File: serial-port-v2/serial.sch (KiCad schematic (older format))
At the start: 25 parts, among them J1 12V Pwr, J2 Serial, J3 XL-320, J4 AX-12A, J5 XL-320, J6 AX-12A, Q1 BSS138, U1 AP1117-50, U2 LM317, U4 74LVC1G126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

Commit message: board fixes
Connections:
- net +3V3: now also Q1.1 (G)
- net at Q1.2 (S), R5.2, U4.2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: no longer Q1.1 (G)
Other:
- moved on the sheet: R5
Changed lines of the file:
@@
 $EndComp
 Wire Wire Line
-	3350 5600 3350 5450
+	3350 5450 3350 5600
 Text GLabel 5350 1000 2    60   Output ~ 0
 RXI
@@
 L +3.3V #PWR027
 U 1 1 5A9E1497
-P 5300 4200
-F 0 "#PWR027" H 5300 4050 50  0001 C CNN
-F 1 "+3.3V" H 5300 4340 50  0000 C CNN
-F 2 "" H 5300 4200 50  0001 C CNN
-F 3 "" H 5300 4200 50  0001 C CNN
-	1    5300 4200
+P 5300 4400
+F 0 "#PWR027" H 5300 4250 50  0001 C CNN
+F 1 "+3.3V" H 5300 4540 50  0000 C CNN
+F 2 "" H 5300 4400 50  0001 C CNN
+F 3 "" H 5300 4400 50  0001 C CNN
+	1    5300 4400
 	-1   0    0    -1
 $EndComp
@@
 L R R5
 U 1 1 5A9E149D
-P 5300 4450
-F 0 "R5" V 5380 4450 50  0000 C CNN
-F 1 "10k" V 5300 4450 50  0000 C CNN
-F 2 "Resistors_SMD:R_1206_HandSoldering" V 5230 4450 50  0001 C CNN
-F 3 "" H 5300 4450 50  0001 C CNN
-	1    5300 4450
+P 5300 4750
+F 0 "R5" V 5380 4750 50  0000 C CNN
+F 1 "10k" V 5300 4750 50  0000 C CNN
+F 2 "Resistors_SMD:R_1206_HandSoldering" V 5230 4750 50  0001 C CNN
+F 3 "" H 5300 4750 50  0001 C CNN
+	1    5300 4750
 	-1   0    0    -1
 $EndComp
@@
 	5250 5000 5450 5000
 Wire Wire Line
-	5300 4200 5300 4300
-Wire Wire Line
-	5300 4600 5300 5000
+	5300 4400 5300 4600
+Wire Wire Line
+	5300 4900 5300 5000
 Connection ~ 5300 5000
 Wire Wire Line
-	5050 4700 5050 4650
-Wire Wire Line
-	5050 4650 5300 4650
-Connection ~ 5300 4650
+	5050 4500 5050 4700
 Wire Wire Line
 	4650 5000 4850 5000
@@
 	3600 5550 3350 5550
 Connection ~ 3350 5550
+Wire Wire Line
+	5050 4500 5300 4500
+Connection ~ 5300 4500
 $EndSCHEMATC

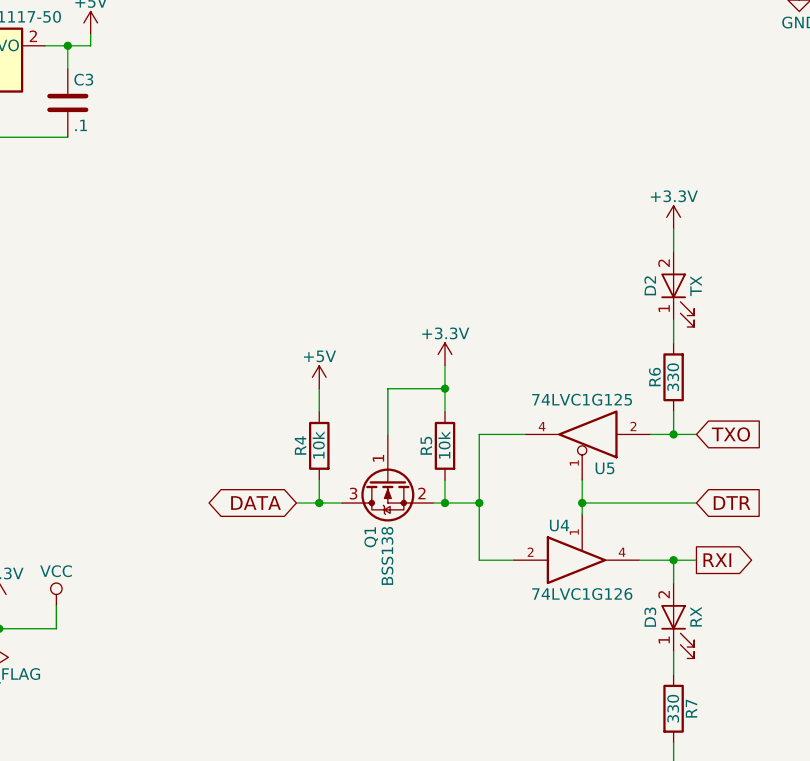
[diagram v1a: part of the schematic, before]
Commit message: mosfet fix?
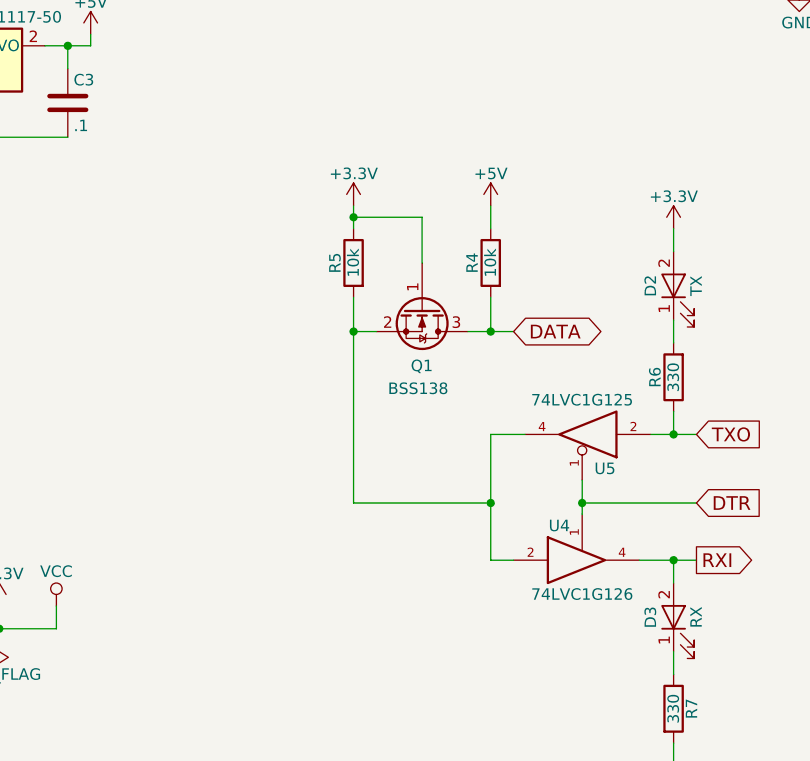
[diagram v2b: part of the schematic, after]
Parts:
- Q1: footprint TO_SOT_Packages_SMD:SOT-23_Handsoldering -> TO_SOT_Packages_SMD:SOT-23
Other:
- moved on the sheet: R4, R5
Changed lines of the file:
@@
 	-1   0    0    1
 $EndComp
-Text GLabel 4650 5000 0    60   BiDi ~ 0
+Text GLabel 5600 4250 2    60   BiDi ~ 0
 DATA
 Text GLabel 6400 5000 2    60   Input ~ 0
@@
 L +3.3V #PWR027
 U 1 1 5A9E1497
-P 5300 4400
-F 0 "#PWR027" H 5300 4250 50  0001 C CNN
-F 1 "+3.3V" H 5300 4540 50  0000 C CNN
-F 2 "" H 5300 4400 50  0001 C CNN
-F 3 "" H 5300 4400 50  0001 C CNN
-	1    5300 4400
+P 4900 3700
+F 0 "#PWR027" H 4900 3550 50  0001 C CNN
+F 1 "+3.3V" H 4900 3840 50  0000 C CNN
+F 2 "" H 4900 3700 50  0001 C CNN
+F 3 "" H 4900 3700 50  0001 C CNN
+	1    4900 3700
 	-1   0    0    -1
 $EndComp
@@
 L R R5
 U 1 1 5A9E149D
-P 5300 4750
-F 0 "R5" V 5380 4750 50  0000 C CNN
-F 1 "10k" V 5300 4750 50  0000 C CNN
-F 2 "Resistors_SMD:R_1206_HandSoldering" V 5230 4750 50  0001 C CNN
-F 3 "" H 5300 4750 50  0001 C CNN
-	1    5300 4750
+P 4900 3950
+F 0 "R5" V 4980 3950 50  0000 C CNN
+F 1 "10k" V 4900 3950 50  0000 C CNN
+F 2 "Resistors_SMD:R_1206_HandSoldering" V 4830 3950 50  0001 C CNN
+F 3 "" H 4900 3950 50  0001 C CNN
+	1    4900 3950
 	-1   0    0    -1
 $EndComp
@@
 L +5V #PWR028
 U 1 1 5A9E14A3
-P 4750 4500
-F 0 "#PWR028" H 4750 4350 50  0001 C CNN
-F 1 "+5V" H 4750 4640 50  0000 C CNN
-F 2 "" H 4750 4500 50  0001 C CNN
-F 3 "" H 4750 4500 50  0001 C CNN
-	1    4750 4500
+P 5500 3700
+F 0 "#PWR028" H 5500 3550 50  0001 C CNN
+F 1 "+5V" H 5500 3840 50  0000 C CNN
+F 2 "" H 5500 3700 50  0001 C CNN
+F 3 "" H 5500 3700 50  0001 C CNN
+	1    5500 3700
 	-1   0    0    -1
 $EndComp
@@
 L R R4
 U 1 1 5A9E14A9
-P 4750 4750
-F 0 "R4" V 4830 4750 50  0000 C CNN
-F 1 "10k" V 4750 4750 50  0000 C CNN
-F 2 "Resistors_SMD:R_1206_HandSoldering" V 4680 4750 50  0001 C CNN
-F 3 "" H 4750 4750 50  0001 C CNN
-	1    4750 4750
-	-1   0    0    -1
-$EndComp
-Wire Wire Line
-	5250 5000 5450 5000
-Wire Wire Line
-	5300 4400 5300 4600
-Wire Wire Line
-	5300 4900 5300 5000
-Connection ~ 5300 5000
-Wire Wire Line
-	5050 4500 5050 4700
-Wire Wire Line
-	4650 5000 4850 5000
-Wire Wire Line
-	4750 4900 4750 5000
-Connection ~ 4750 5000
-Wire Wire Line
-	4750 4600 4750 4500
-Wire Wire Line
-	5450 5250 5600 5250
-Wire Wire Line
-	5450 4700 5450 5250
-Wire Wire Line
-	5650 4700 5450 4700
-Connection ~ 5450 5000
+P 5500 3950
+F 0 "R4" V 5580 3950 50  0000 C CNN
+F 1 "10k" V 5500 3950 50  0000 C CNN
+F 2 "Resistors_SMD:R_1206_HandSoldering" V 5430 3950 50  0001 C CNN
+F 3 "" H 5500 3950 50  0001 C CNN
+	1    5500 3950
+	-1   0    0    -1
+$EndComp
 Wire Wire Line
 	6400 5000 5900 5000
@@
 	6900 1450 6750 1450
 Connection ~ 6750 1450
-$Comp
-L BSS138 Q1
-U 1 1 5A9E5356
-P 5050 4900
-F 0 "Q1" H 5250 4975 50  0000 L CNN
-F 1 "BSS138" H 5250 4900 50  0000 L CNN
-F 2 "TO_SOT_Packages_SMD:SOT-23_Handsoldering" H 5250 4825 50  0001 L CIN
-F 3 "" H 5050 4900 50  0001 L CNN
-	1    5050 4900
-	0    -1   1    0
-$EndComp
 Wire Wire Line
 	3600 5450 3600 5550
@@
 Connection ~ 3350 5550
 Wire Wire Line
-	5050 4500 5300 4500
-Connection ~ 5300 4500
+	4900 3800 4900 3700
+Wire Wire Line
+	5500 3700 5500 3800
+Wire Wire Line
+	5200 3950 5200 3750
+Wire Wire Line
+	5200 3750 4900 3750
+Connection ~ 4900 3750
+Wire Wire Line
+	4900 4100 4900 5000
+Wire Wire Line
+	4900 4250 5000 4250
+Wire Wire Line
+	5400 4250 5600 4250
+Wire Wire Line
+	5500 4100 5500 4250
+Connection ~ 5500 4250
+Wire Wire Line
+	5650 4700 5500 4700
+Wire Wire Line
+	5500 4700 5500 5250
+Wire Wire Line
+	5500 5250 5600 5250
+Wire Wire Line
+	4900 5000 5500 5000
+Connection ~ 5500 5000
+Connection ~ 4900 4250
+$Comp
+L BSS138 Q1
+U 1 1 5AADA99E
+P 5200 4150
+F 0 "Q1" V 5450 4100 50  0000 L CNN
+F 1 "BSS138" V 5550 4000 50  0000 L CNN
+F 2 "TO_SOT_Packages_SMD:SOT-23" H 5400 4075 50  0001 L CIN
+F 3 "" H 5200 4150 50  0001 L CNN
+	1    5200 4150
+	0    1    1    0
+$EndComp
 $EndSCHEMATC
